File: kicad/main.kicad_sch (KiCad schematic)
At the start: 41 parts, among them J1 Jack-DC, J2 LCD, J3 Addr, J4 IO~{EN}_{[2..7]}, J5 Data, J6 Control, J7 VIA_A, J8 VIA_B, SW1 Step, SW2 Reset, X1 1 MHz

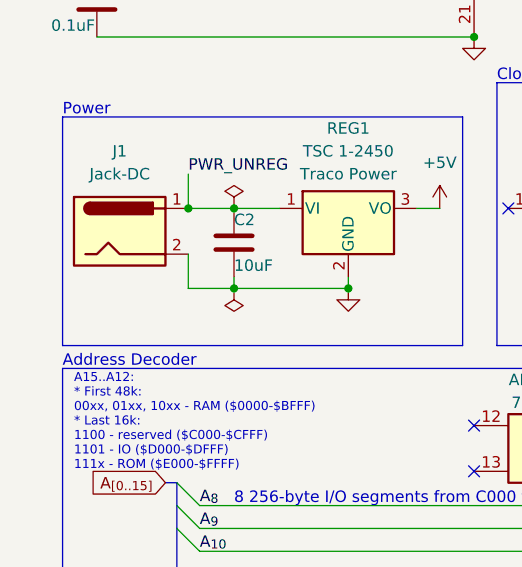
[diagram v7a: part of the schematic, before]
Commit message: Add standoffs, update V9 render
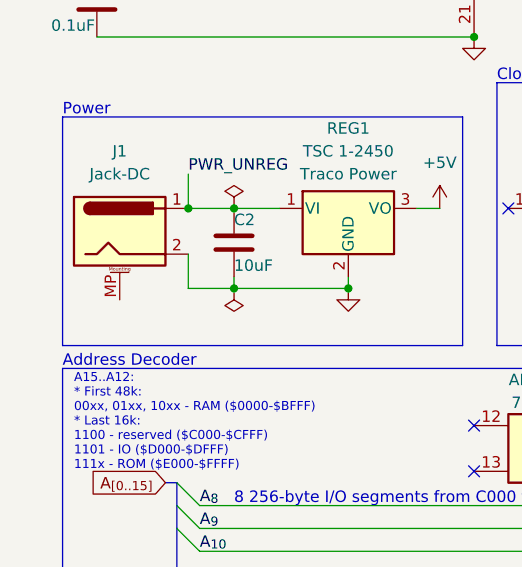
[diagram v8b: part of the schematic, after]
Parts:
- removed J1: Jack-DC, Connector_BarrelJack:BarrelJack_GCT_DCJ200-10-A_Horizontal, symbol Connector:Jack-DC
- added J1: Jack-DC, Connector_BarrelJack:BarrelJack_GCT_DCJ200-10-A_Horizontal, symbol Connector:Barrel_Jack_MountingPin
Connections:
- net GND: now also J1.2
- net PWR_UNREG: now also J1.1
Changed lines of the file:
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@@
   (junction (at 80.01 168.91) (diameter 0) (color 0 0 0 0)
   )
-  (junction (at 29.21 118.11) (diameter 0) (color 0 0 0 0)
-  )
   (junction (at 210.82 152.4) (diameter 0) (color 0 0 0 0)
   )
@@
   (junction (at 153.67 147.32) (diameter 0) (color 0 0 0 0)
   )
+  (junction (at 29.21 118.11) (diameter 0) (color 0 0 0 0)
+  )
   (junction (at 101.6 71.12) (diameter 0) (color 0 0 0 0)
   )
@@
   (symbol (lib_id "power:GND") (at 269.24 97.79 0) (unit 1)
     (in_bom yes) (on_board yes) (fields_autoplaced)
-    (property "Reference" "#PWR034" (id 0) (at 269.24 104.14 0)
+    (property "Reference" "#PWR032" (id 0) (at 269.24 104.14 0)
       (effects (font (size 1.27 1.27)) hide)
     )
@@
     (pin "1")
   )
+  (symbol (lib_id "Connector:Barrel_Jack_MountingPin") (at 21.59 120.65 0) (unit 1)
+    (in_bom yes) (on_board yes) (fields_autoplaced)
+    (property "Reference" "J1" (id 0) (at 21.59 111.76 0))
+    (property "Value" "Jack-DC" (id 1) (at 21.59 114.3 0))
+    (property "Footprint" "Connector_BarrelJack:BarrelJack_GCT_DCJ200-10-A_Horizontal" (id 2) (at 22.86 121.666 0)
+      (effects (font (size 1.27 1.27)) hide)
+    )
+    (property "Datasheet" "~" (id 3) (at 22.86 121.666 0)
+      (effects (font (size 1.27 1.27)) hide)
+    )
+    (pin "1")
+    (pin "2")
+    (pin "MP")
+  )
   (symbol (lib_id "65xx:W65C02SxP") (at 60.96 59.69 0) (unit 1)
     (in_bom yes) (on_board yes) (fields_autoplaced)
@@
   (symbol (lib_id "power:GND") (at 179.07 154.94 0) (unit 1)
     (in_bom yes) (on_board yes)
-    (property "Reference" "#PWR022" (id 0) (at 179.07 161.29 0)
+    (property "Reference" "#PWR024" (id 0) (at 179.07 161.29 0)
       (effects (font (size 1.27 1.27)) hide)
     )
@@
   (symbol (lib_id "power:GND") (at 177.8 78.74 0) (unit 1)
     (in_bom yes) (on_board yes) (fields_autoplaced)
-    (property "Reference" "#PWR024" (id 0) (at 177.8 85.09 0)
+    (property "Reference" "#PWR023" (id 0) (at 177.8 85.09 0)
       (effects (font (size 1.27 1.27)) hide)
     )
@@
     (pin "3")
   )
-  (symbol (lib_id "Connector:Jack-DC") (at 21.59 120.65 0) (unit 1)
-    (in_bom yes) (on_board yes) (fields_autoplaced)
-    (property "Reference" "J1" (id 0) (at 21.59 111.76 0))
-    (property "Value" "Jack-DC" (id 1) (at 21.59 114.3 0))
-    (property "Footprint" "Connector_BarrelJack:BarrelJack_GCT_DCJ200-10-A_Horizontal" (id 2) (at 22.86 121.666 0)
-      (effects (font (size 1.27 1.27)) hide)
-    )
-    (property "Datasheet" "~" (id 3) (at 22.86 121.666 0)
-      (effects (font (size 1.27 1.27)) hide)
-    )
-    (pin "1")
-    (pin "2")
-  )
   (symbol (lib_id "74xx:74HC00") (at 172.72 132.08 0) (unit 3)
     (in_bom yes) (on_board yes) (fields_autoplaced)
@@
   (symbol (lib_id "power:+5V") (at 177.8 22.86 0) (unit 1)
     (in_bom yes) (on_board yes)
-    (property "Reference" "#PWR023" (id 0) (at 177.8 26.67 0)
+    (property "Reference" "#PWR022" (id 0) (at 177.8 26.67 0)
       (effects (font (size 1.27 1.27)) hide)
     )
@@
   (symbol (lib_id "power:+5V") (at 259.08 133.35 0) (unit 1)
     (in_bom yes) (on_board yes)
-    (property "Reference" "#PWR0102" (id 0) (at 259.08 137.16 0)
+    (property "Reference" "#PWR029" (id 0) (at 259.08 137.16 0)
       (effects (font (size 1.27 1.27)) hide)
     )
@@
   (symbol (lib_id "power:+5V") (at 261.62 26.67 0) (unit 1)
     (in_bom yes) (on_board yes)
-    (property "Reference" "#PWR032" (id 0) (at 261.62 30.48 0)
+    (property "Reference" "#PWR030" (id 0) (at 261.62 30.48 0)
       (effects (font (size 1.27 1.27)) hide)
     )
@@
   (symbol (lib_id "power:GND") (at 261.62 160.02 0) (unit 1)
     (in_bom yes) (on_board yes) (fields_autoplaced)
-    (property "Reference" "#PWR0101" (id 0) (at 261.62 166.37 0)
+    (property "Reference" "#PWR031" (id 0) (at 261.62 166.37 0)
       (effects (font (size 1.27 1.27)) hide)
     )
@@
       (reference "#PWR021") (unit 1) (value "GND") (footprint "")
     )
-    (path "/1794ee9e-4a37-4833-88e9-2bff75fa6d3b"
-      (reference "#PWR022") (unit 1) (value "GND") (footprint "")
-    )
     (path "/a3ff685b-9838-4e1f-aa54-181daa6aa5e6"
-      (reference "#PWR023") (unit 1) (value "+5V") (footprint "")
+      (reference "#PWR022") (unit 1) (value "+5V") (footprint "")
     )
     (path "/4f8fdd92-864f-4faa-9083-d45f45542d58"
+      (reference "#PWR023") (unit 1) (value "GND") (footprint "")
+    )
+    (path "/1794ee9e-4a37-4833-88e9-2bff75fa6d3b"
       (reference "#PWR024") (unit 1) (value "GND") (footprint "")
     )
@@
       (reference "#PWR028") (unit 1) (value "GND") (footprint "")
     )
-    (path "/d97d669f-6a81-48f2-95ca-f23da91ea840"
-      (reference "#PWR032") (unit 1) (value "+5V") (footprint "")
+    (path "/a4b57b38-ce4a-4682-9aa0-2bae6cc413c1"
+      (reference "#PWR029") (unit 1) (value "+5V") (footprint "")
     )
-    (path "/04b735e7-abd2-4794-a4a0-24e573787a1f"
-      (reference "#PWR034") (unit 1) (value "GND") (footprint "")
+    (path "/d97d669f-6a81-48f2-95ca-f23da91ea840"
+      (reference "#PWR030") (unit 1) (value "+5V") (footprint "")
     )
     (path "/e2626442-34de-48a8-8792-070f8da0e999"
-      (reference "#PWR0101") (unit 1) (value "GND") (footprint "")
+      (reference "#PWR031") (unit 1) (value "GND") (footprint "")
     )
-    (path "/a4b57b38-ce4a-4682-9aa0-2bae6cc413c1"
-      (reference "#PWR0102") (unit 1) (value "+5V") (footprint "")
+    (path "/04b735e7-abd2-4794-a4a0-24e573787a1f"
+      (reference "#PWR032") (unit 1) (value "GND") (footprint "")
     )
     (path "/2305be88-dd7f-422b-877e-ff83bc42f13e"
@@
       (reference "IO1") (unit 1) (value "74HC138") (footprint "Package_DIP:DIP-16_W7.62mm")
     )
-    (path "/9da8793c-c086-4698-9614-061c1e3b2577"
+    (path "/080fa4a1-0cda-4ba5-aa95-ba6d00209f97"
       (reference "J1") (unit 1) (value "Jack-DC") (footprint "Connector_BarrelJack:BarrelJack_GCT_DCJ200-10-A_Horizontal")
     )
